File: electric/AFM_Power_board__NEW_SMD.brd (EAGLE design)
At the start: 68.2 x 57.1 mm, 31 parts, among them IC2 7815DT, IC4 7805DT, J1 POWER_JACKPOWER_JACK_SLOT, U2 LTC3260EMSE#PBF

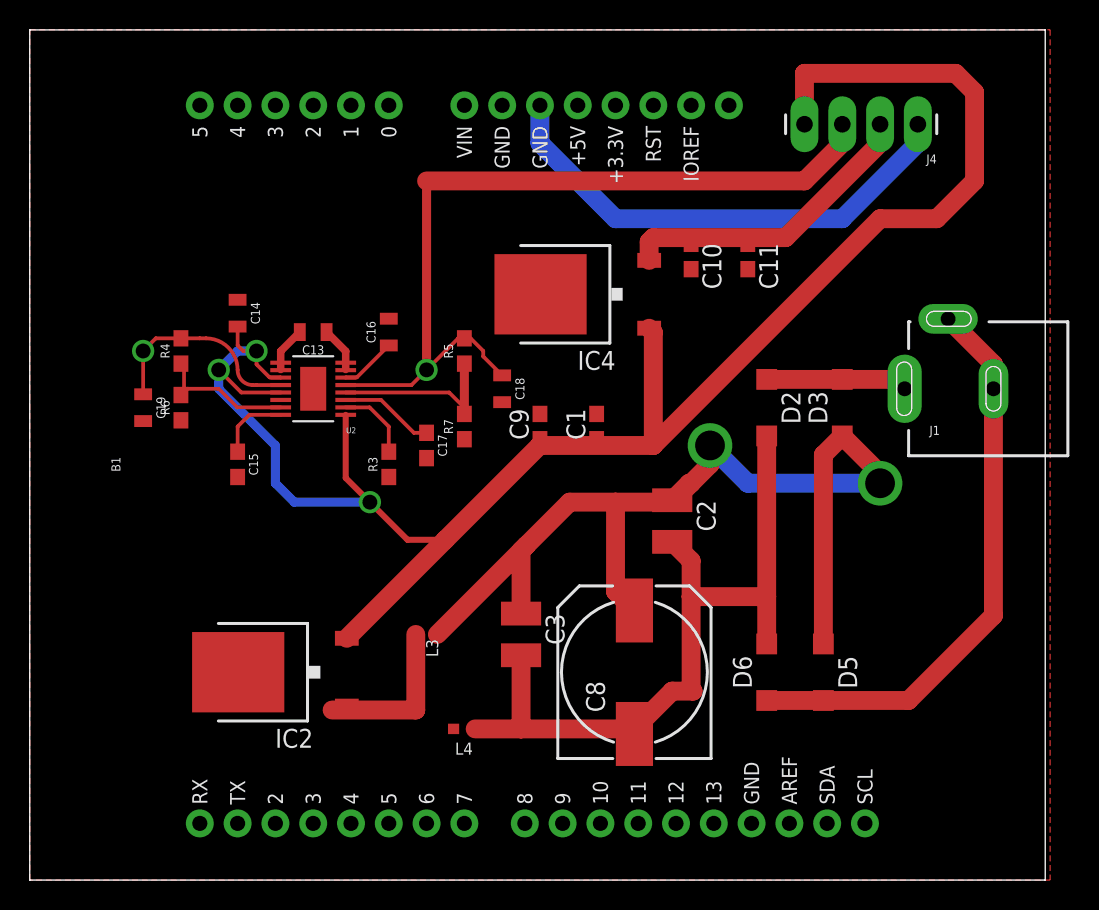
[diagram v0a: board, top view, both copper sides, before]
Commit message: Updated to boards. Changes reflects fixes needed to PCBWay boards
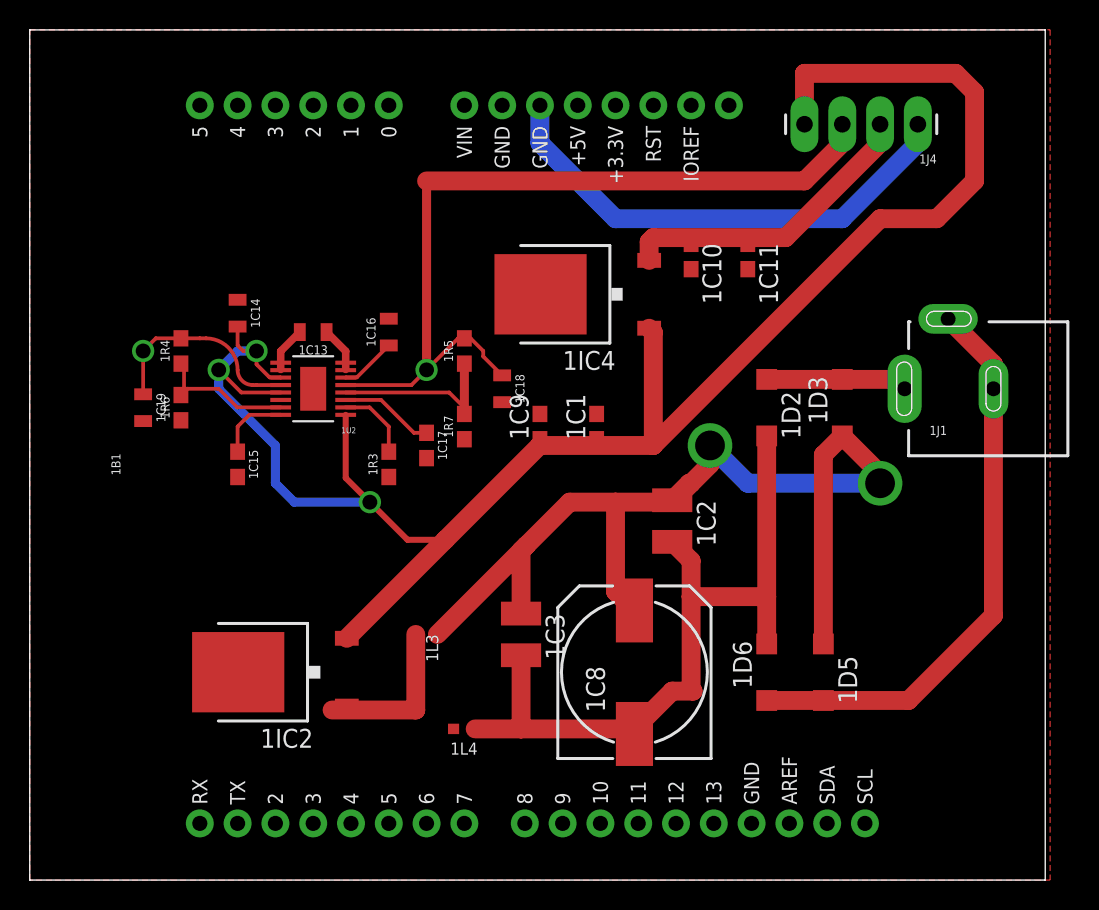
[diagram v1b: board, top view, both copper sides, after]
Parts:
- 1R4, 1R5: value 100k -> 910k
- renumbered B1 to 1B1, C1 to 1C1, C10 to 1C10, C11 to 1C11, C13 to 1C13, C14 to 1C14, C15 to 1C15, C16 to 1C16, C17 to 1C17, C18 to 1C18, C19 to 1C19, C2 to 1C2, C3 to 1C3, C8 to 1C8, C9 to 1C9, D2 to 1D2, D3 to 1D3, D5 to 1D5, D6 to 1D6, IC2 to 1IC2, IC4 to 1IC4, J1 to 1J1, J4 to 1J4, L3 to 1L3, L4 to 1L4, R3 to 1R3, R4 to 1R4, R5 to 1R5, R6 to 1R6, R7 to 1R7, U2 to 1U2
